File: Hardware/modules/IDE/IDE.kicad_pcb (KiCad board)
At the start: 4 copper layers, 83.3 x 68.2 mm, 22 parts, among them J1 Conn_02x20_Odd_Even, J2 IDE_VCC, J3 Conn_02x22_Odd_Even, J4 Bus_PCI_6502, U1 74AHC1G00, U2 6525, U3 74HCT04, U4 74HC138

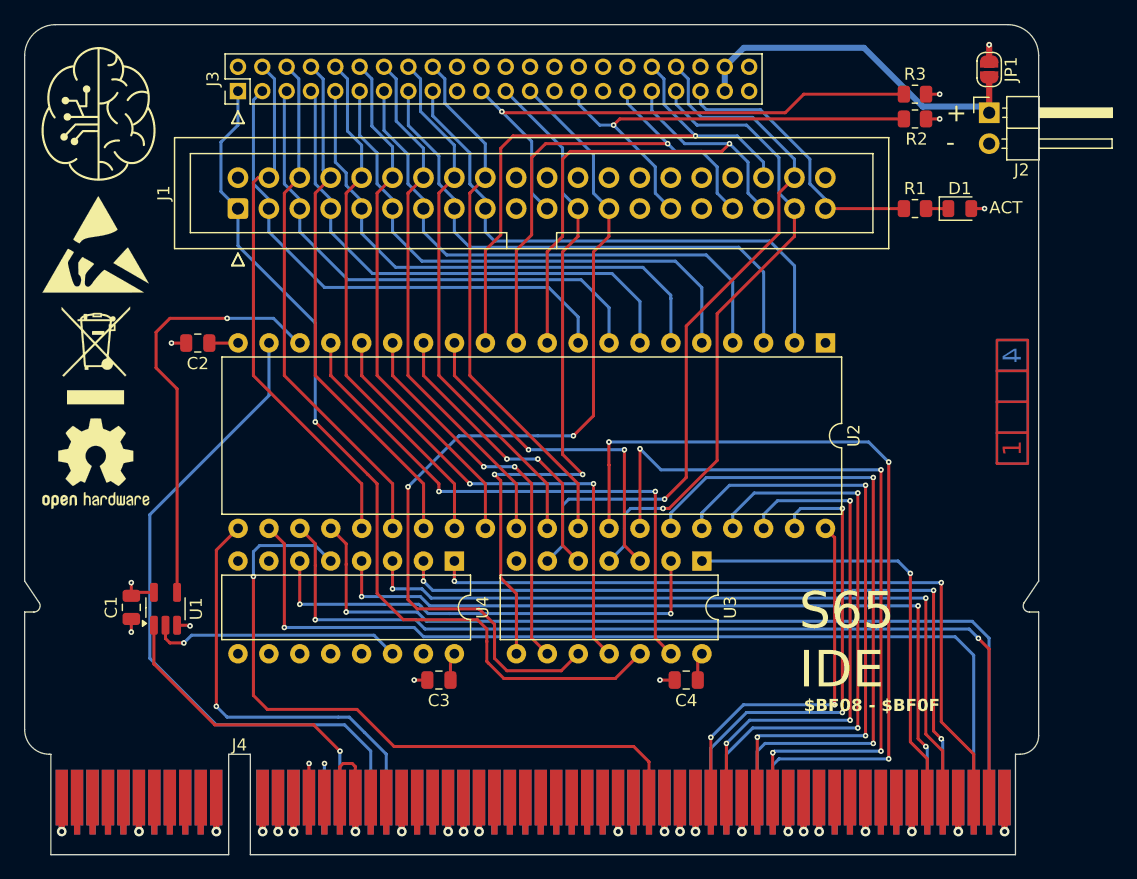
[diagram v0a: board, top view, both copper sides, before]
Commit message: Hardware Update Add MyCPU VGA Module Beautify all Schematics minor Error corrections Readme Update
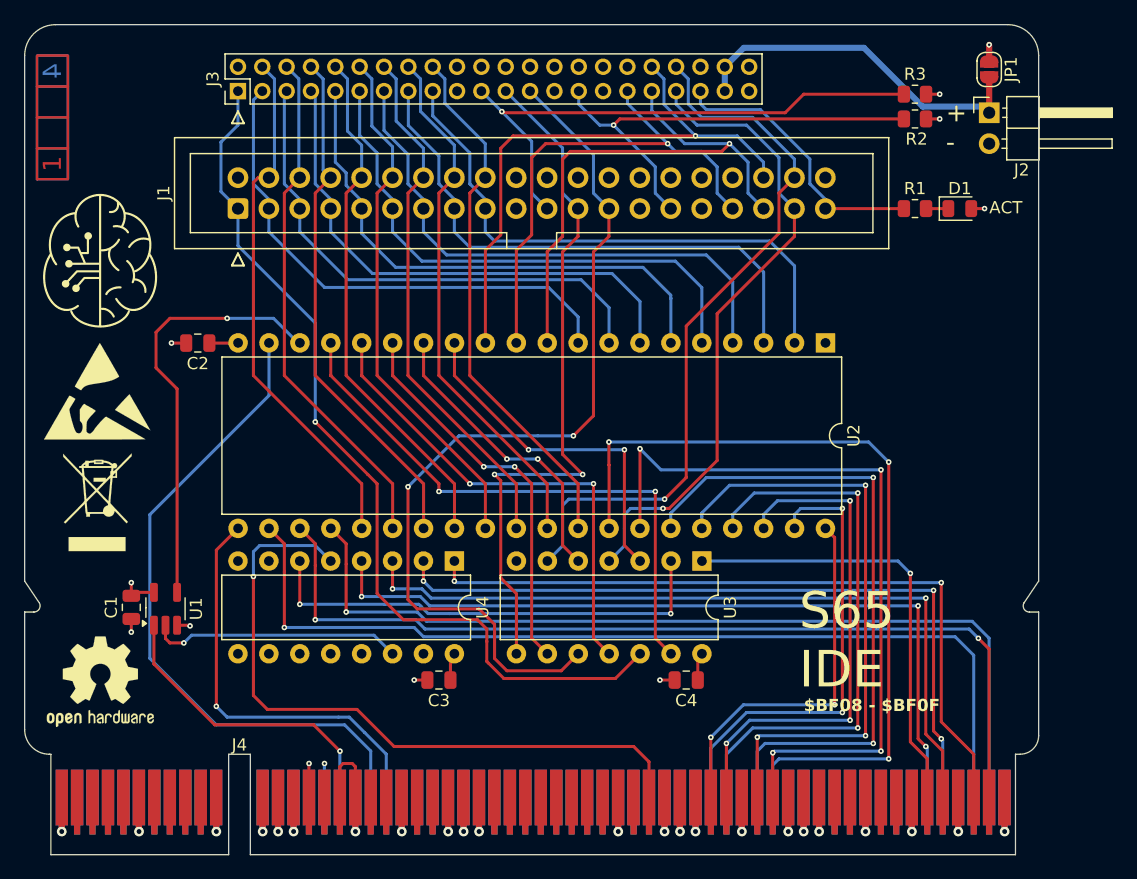
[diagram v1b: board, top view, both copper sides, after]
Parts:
- moved Ref** 82.3 mm to (114.4, 66.4)
- moved REF** 17.9 mm to (118.4, 112.8)
- moved REF** 12.1 mm to (118.1, 88.9)
- moved G*** 12.1 mm to (118.4, 78.2)
- moved REF** 12.1 mm to (118.1, 98.0)
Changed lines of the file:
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@@
 	(footprint "Symbol:ESD-Logo_8.9x8mm_SilkScreen"
 		(layer "F.Cu")
-		(at 117.983 76.835)
+		(at 118.11 88.9)
 		(descr "Electrostatic discharge Logo")
 		(tags "Logo ESD")
@@
 	(footprint "Symbol:OSHW-Logo2_9.8x8mm_SilkScreen"
 		(layer "F.Cu")
-		(at 117.983 94.869)
+		(at 118.364 112.776)
 		(descr "Open Source Hardware Symbol")
 		(tags "Logo Symbol OSHW")
@@
 	(footprint "Eigene:ladder_4"
 		(layer "F.Cu")
-		(at 193.294 89.789 90)
+		(at 114.427 66.421 90)
 		(property "Reference" "Ref**"
 			(at 0 0 90)
@@
 	(footprint "Eigene:logo"
 		(layer "F.Cu")
-		(at 118.237 66.167)
+		(at 118.364 78.232)
 		(property "Reference" "G***"
 			(at 0 0 0)
@@
 	(footprint "Symbol:WEEE-Logo_5.6x8mm_SilkScreen"
 		(layer "F.Cu")
-		(at 117.983 85.979)
+		(at 118.11 98.044)
 		(descr "Waste Electrical and Electronic Equipment Directive")
 		(tags "Logo WEEE")

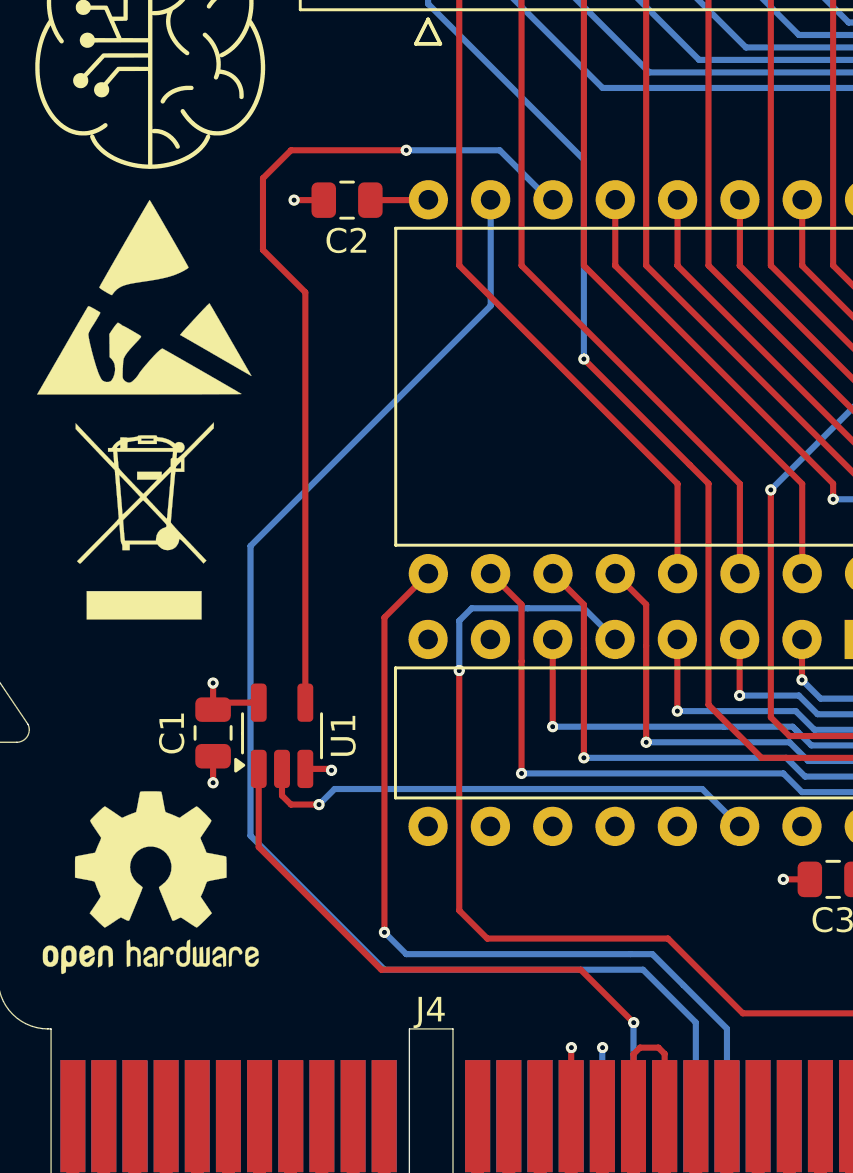
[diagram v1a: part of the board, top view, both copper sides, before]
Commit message: Chip Select Strobe Generation Bugfix
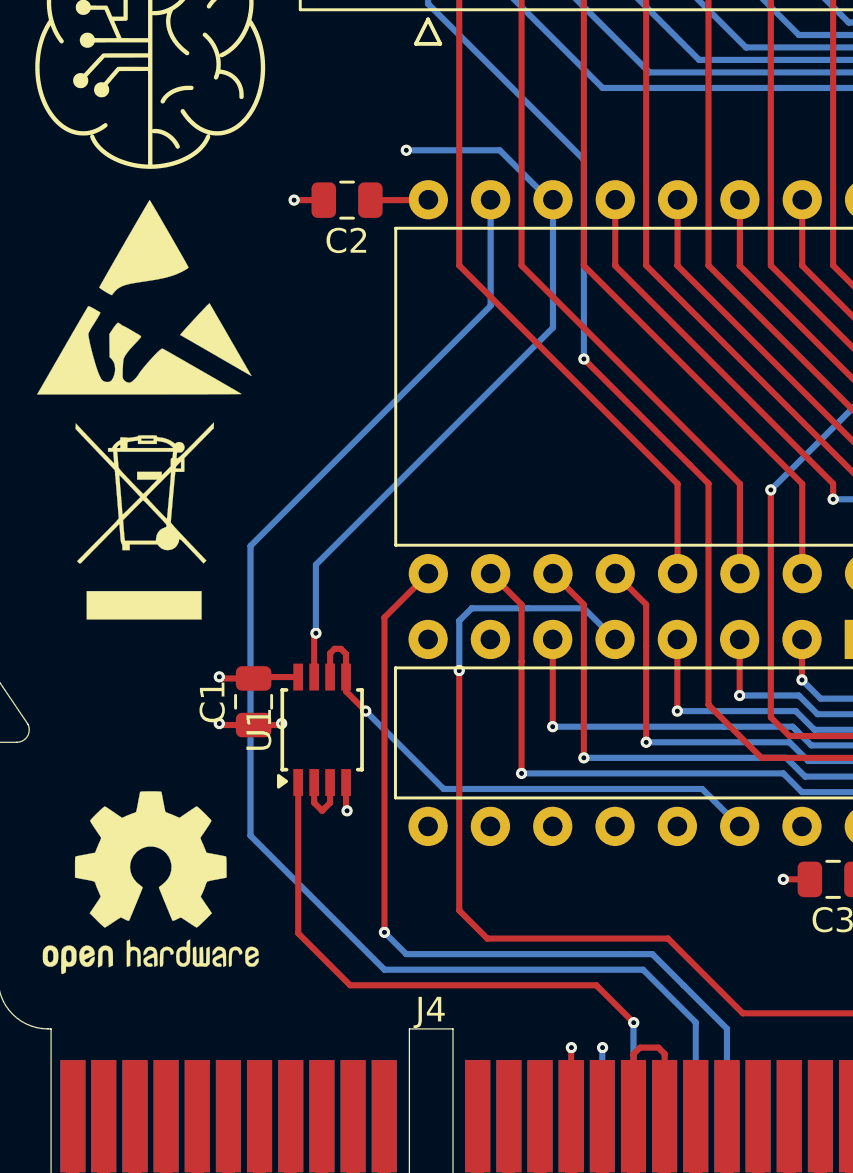
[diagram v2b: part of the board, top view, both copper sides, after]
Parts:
- U1: value 74AHC1G00 -> 74AHC2G00; footprint Package_TO_SOT_SMD:SOT-23-5_HandSoldering -> Package_SO:TSSOP-8_3x3mm_P0.65mm
- moved C1 2.08 mm to (122.6, 105.4)
- moved U1 1.65 mm to (125.3, 106.6)
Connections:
- D1 pad 1: Net-(D1-K) -> (no net)
- J1 pad 20: unconnected-(J1-Pin_20-Pad20) -> (no net)
- J1 pad 27: unconnected-(J1-Pin_27-Pad27) -> (no net)
- J1 pad 31: unconnected-(J1-Pin_31-Pad31) -> (no net)
- J1 pad 32: unconnected-(J1-Pin_32-Pad32) -> (no net)
- J1 pad 34: unconnected-(J1-Pin_34-Pad34) -> (no net)
- J3 pad 20: unconnected-(J3-Pin_20-Pad20) -> (no net)
- J3 pad 27: unconnected-(J3-Pin_27-Pad27) -> (no net)
- J3 pad 31: unconnected-(J3-Pin_31-Pad31) -> (no net)
- J3 pad 32: unconnected-(J3-Pin_32-Pad32) -> (no net)
- J3 pad 34: unconnected-(J3-Pin_34-Pad34) -> (no net)
- J4 pad A11: /A13 -> (no net)
- J4 pad A12: /A15 -> (no net)
- J4 pad A25: /~{ROM} -> (no net)
- J4 pad A27: /~{IRQ_0.0} -> (no net)
- J4 pad A28: /~{IRQ_0.1} -> (no net)
- J4 pad A29: /~{IRQ_0.2} -> (no net)
- J4 pad A30: /~{IRQ_0.3} -> (no net)
- J4 pad A31: /~{IRQ_0.4} -> (no net)
- J4 pad A32: /~{IRQ_0.5} -> (no net)
- J4 pad A33: /~{IRQ_0.6} -> (no net)
- J4 pad A34: /~{IRQ_0.7} -> (no net)
- J4 pad A38: /SYNC_VPA -> (no net)
- J4 pad A39: /Ø2/VDA -> (no net)
- J4 pad A41: /~{RDY} -> (no net)
- J4 pad A42: /~{BE} -> (no net)
- J4 pad A45: /E -> (no net)
- J4 pad A53: /RAM_0 -> (no net)
- J4 pad A54: /RAM_1 -> (no net)
- J4 pad A55: /RAM_2 -> (no net)
- J4 pad A56: /RAM_3 -> (no net)
- J4 pad A58: /RAM_4 -> (no net)
- J4 pad A59: /RAM_5 -> (no net)
- J4 pad A60: /RAM_6 -> (no net)
- J4 pad A61: /RAM_7 -> (no net)
- J4 pad A8: /A9 -> (no net)
- J4 pad A9: /A11 -> (no net)
- J4 pad B11: /A12 -> (no net)
- J4 pad B12: /A14 -> (no net)
- J4 pad B24: /~{L_RAM} -> (no net)
- J4 pad B25: /~{H_RAM} -> (no net)
- J4 pad B27: /~{IRQ} -> (no net)
- J4 pad B28: /~{IRQ_0} -> (no net)
- J4 pad B29: /~{IRQ_1} -> (no net)
- J4 pad B30: /~{IRQ_2} -> (no net)
- J4 pad B31: /~{IRQ_3} -> (no net)
- J4 pad B32: /~{IRQ_4} -> (no net)
- J4 pad B33: /~{NMI} -> (no net)
- J4 pad B34: /PAGE -> (no net)
- J4 pad B38: /~{VP} -> (no net)
- J4 pad B39: /~{ML} -> (no net)
- J4 pad B46: /M/X -> (no net)
- J4 pad B53: /ROM_0 -> (no net)
- J4 pad B54: /ROM_1 -> (no net)
- J4 pad B55: /ROM_2 -> (no net)
- J4 pad B56: /ROM_3 -> (no net)
- J4 pad B58: /ROM_4 -> (no net)
- J4 pad B59: /ROM_5 -> (no net)
- J4 pad B60: /ROM_6 -> (no net)
- J4 pad B61: /ROM_7 -> (no net)
- J4 pad B8: /A8 -> (no net)
- J4 pad B9: /A10 -> (no net)
- R1 pad 2: Net-(D1-K) -> (no net)
- U1 pad 3: GND -> /PORT_8
- U1 pad 4: Net-(U2-~{CS}) -> GND
- U1 pad 5: +5V -> Net-(U1-Pad5)
- U2 pad 13: Net-(U2-PB3) -> (no net)
- U2 pad 14: Net-(U2-PB4) -> (no net)
- U2 pad 15: Net-(U2-PB5) -> (no net)
- U2 pad 16: Net-(U2-PB6) -> (no net)
- U2 pad 17: Net-(U2-PB7) -> (no net)
- U2 pad 18: Net-(U2-~{CS}) -> unconnected-(U1-Pad7)
- U3 pad 11: Net-(U2-PB6) -> (no net)
- U3 pad 13: Net-(U2-PB7) -> (no net)
- U3 pad 2: Net-(U4-E2) -> (no net)
- U3 pad 3: Net-(U2-PB3) -> (no net)
- U3 pad 5: Net-(U2-PB4) -> (no net)
- U3 pad 9: Net-(U2-PB5) -> (no net)
- U4 pad 10: unconnected-(U4-~{Y5}-Pad10) -> (no net)
- U4 pad 11: unconnected-(U4-~{Y4}-Pad11) -> (no net)
- U4 pad 12: unconnected-(U4-~{Y3}-Pad12) -> (no net)
- U4 pad 13: unconnected-(U4-~{Y2}-Pad13) -> (no net)
- U4 pad 14: /PORT_8 -> Net-(U1-Pad5)
- U4 pad 15: unconnected-(U4-~{Y0}-Pad15) -> (no net)
- U4 pad 6: Net-(U4-E2) -> (no net)
- U4 pad 7: unconnected-(U4-~{Y7}-Pad7) -> (no net)
- U4 pad 9: unconnected-(U4-~{Y6}-Pad9) -> (no net)
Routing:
- net (no net): track 0.00 -> 214.0 mm, vias 0 -> 12
- net Net-(U2-PB7): track 47.5 -> 0.00 mm, vias 2 -> 0
- net Net-(U2-PB6): track 39.9 -> 0.00 mm, vias 2 -> 0
- net Net-(U4-E2): track 38.9 -> 0.00 mm, vias 2 -> 0
- net Net-(U2-~{CS}): track 35.2 -> 0.00 mm, vias 1 -> 0
- net Net-(U2-PB5): track 32.3 -> 0.00 mm, vias 2 -> 0
- net unconnected-(U1-Pad7): track 0.00 -> 30.3 mm, vias 0 -> 2
- net Net-(U2-PB3): track 28.9 -> 0.00 mm, vias 2 -> 0
- net Net-(U2-PB4): track 24.7 -> 0.00 mm, vias 2 -> 0
- net Net-(U1-Pad5): track 0.00 -> 21.6 mm, vias 0 -> 1
- net /PORT_8: track 20.8 -> 2.57 mm, vias 1 -> 0
- net Net-(D1-K): track 1.83 -> 0.00 mm
- net GND: track 18.9 -> 20.5 mm, vias 26 -> 27

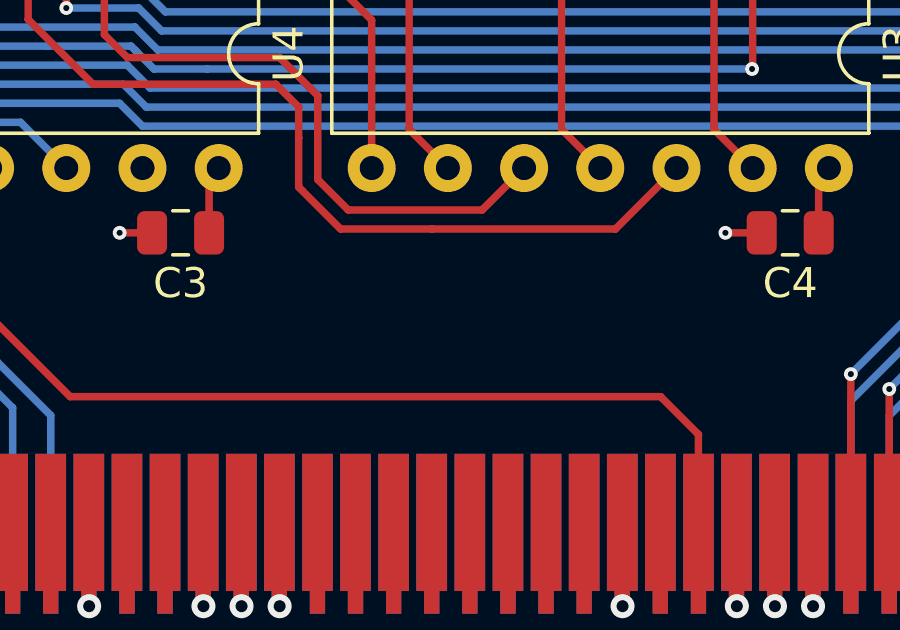
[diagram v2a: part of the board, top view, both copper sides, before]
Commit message: Hardware Review Pt. 1 fix Address Decoding for Strobe Generators add bulk capacitance to every board fix wiring of Prototyping Board
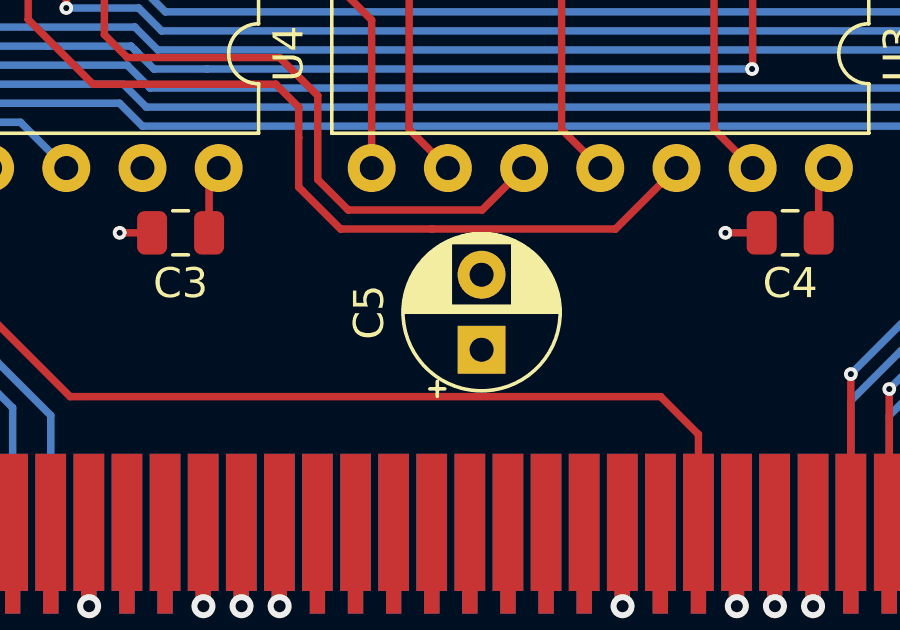
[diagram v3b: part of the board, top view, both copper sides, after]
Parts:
- added C5: 10µ, Capacitor_THT:CP_Radial_D5.0mm_P2.50mm, F.Cu at (156.2, 116.5)

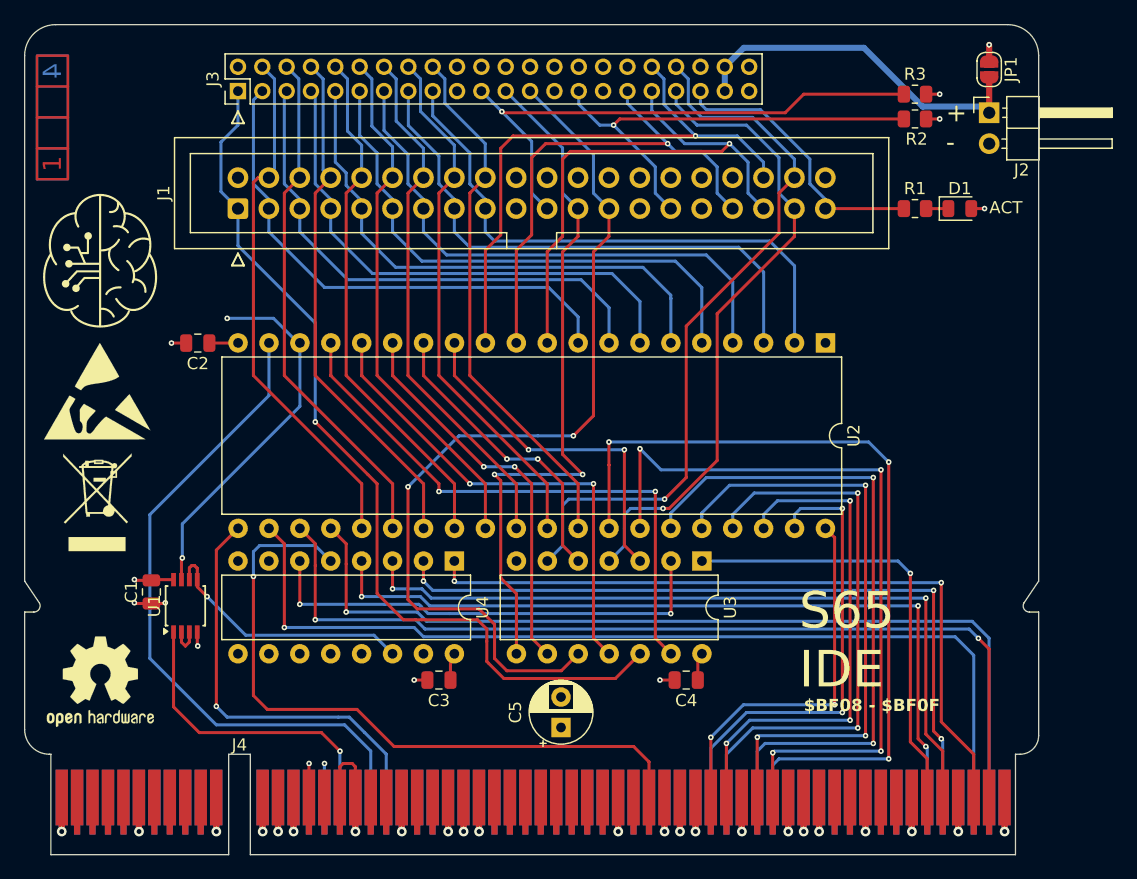
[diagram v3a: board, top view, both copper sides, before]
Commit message: Big Review Update - Changed Copper Pours on all PCBs - Implemented errors found at review - fixed some additional errors
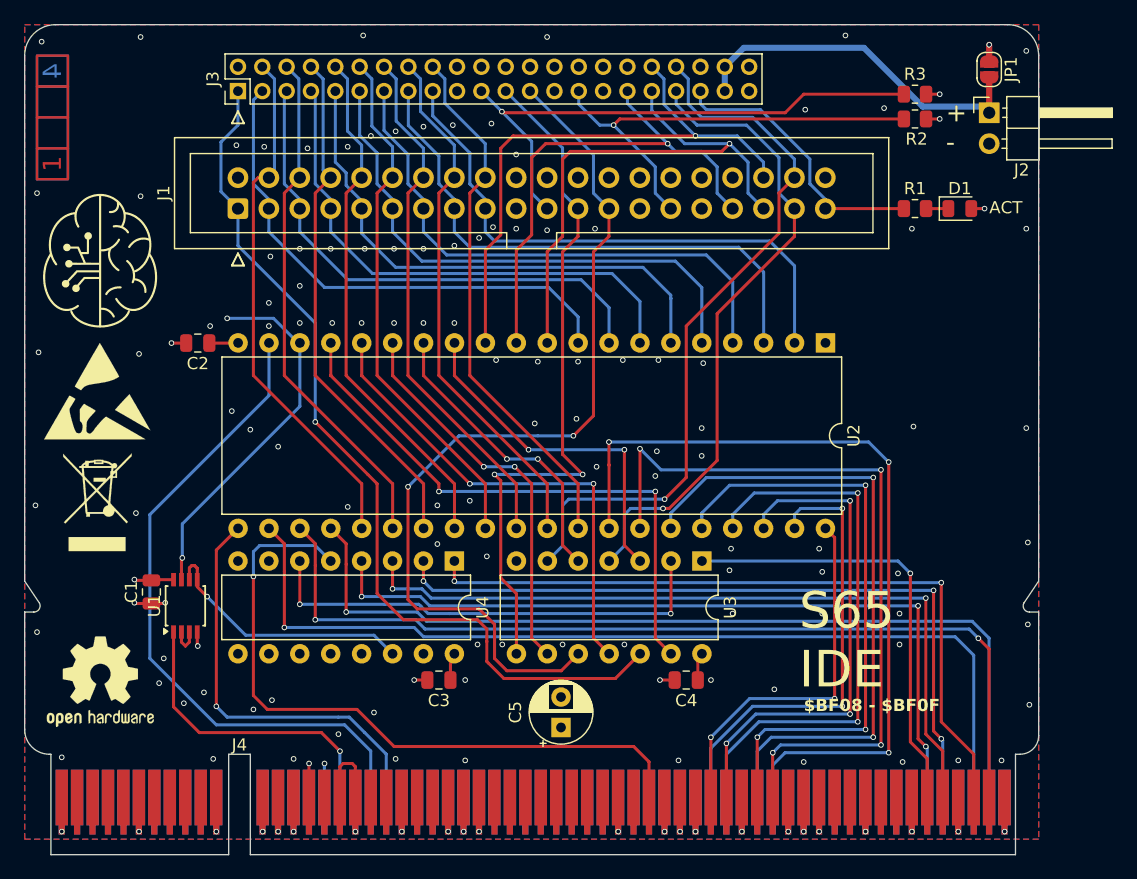
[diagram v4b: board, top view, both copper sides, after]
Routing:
- net +5V: vias 8 -> 117
- added copper zone on B.Cu, net +5V
- added copper zone on F.Cu, net +5V
- added copper zone on In1.Cu, net GND
- removed copper zone on In1.Cu, net +5V
